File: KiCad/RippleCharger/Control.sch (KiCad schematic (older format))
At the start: 13 parts, among them J3 UART1, J4 UART2, U7 LAUNCHXL-F280049C

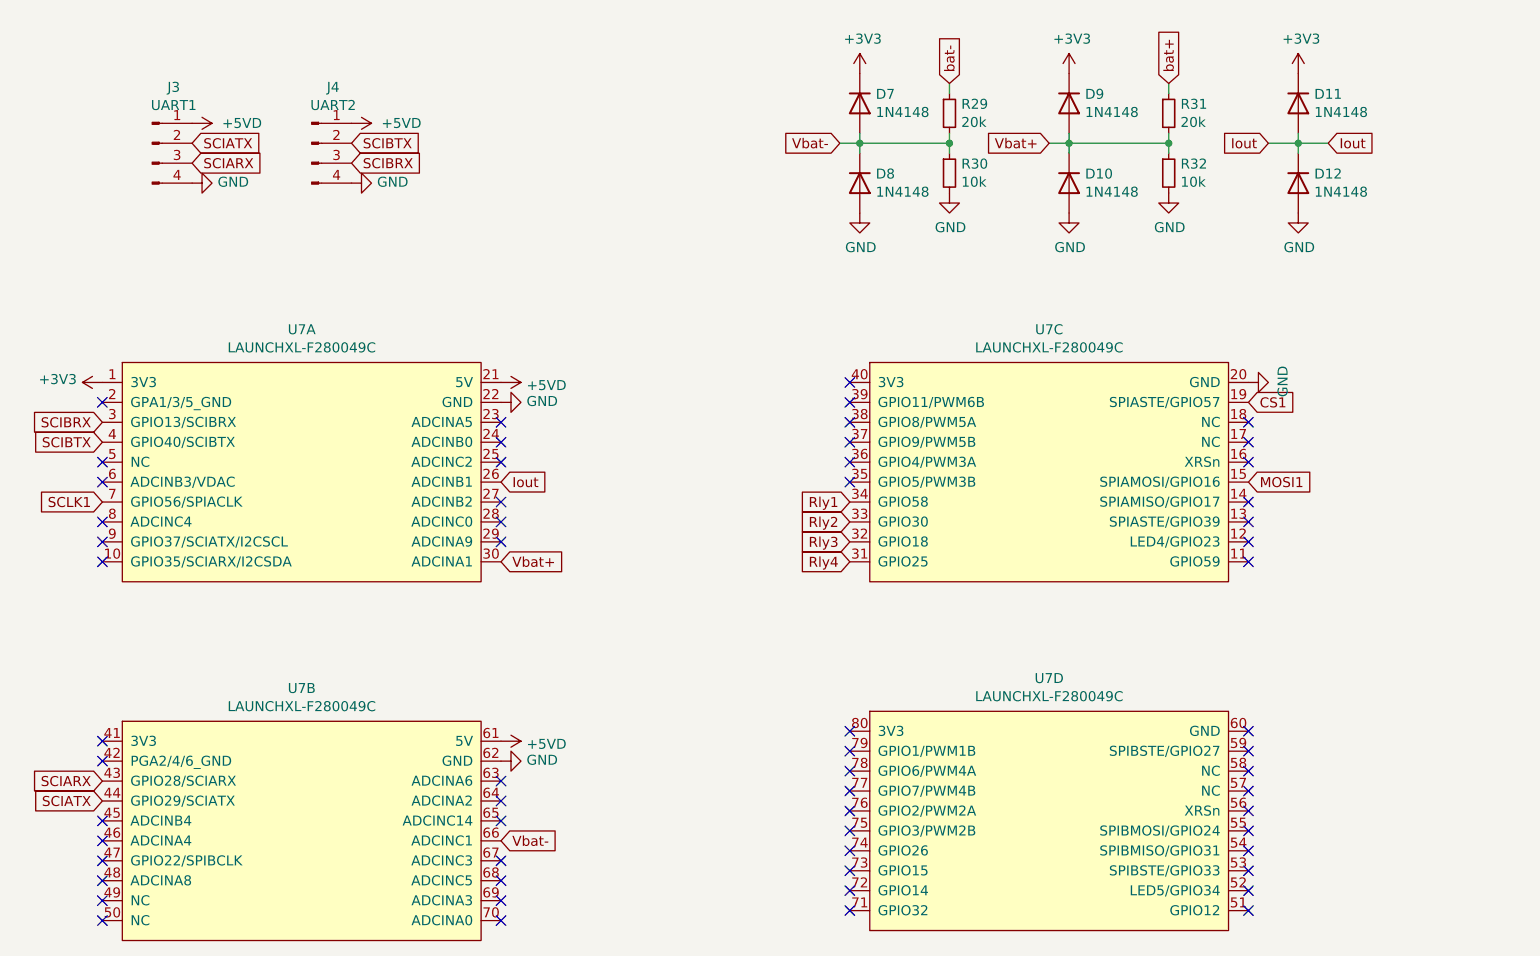
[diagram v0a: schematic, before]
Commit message: Update PCB layout m include relay footprint, board outlook.Modify Main 0049 code and add CV function
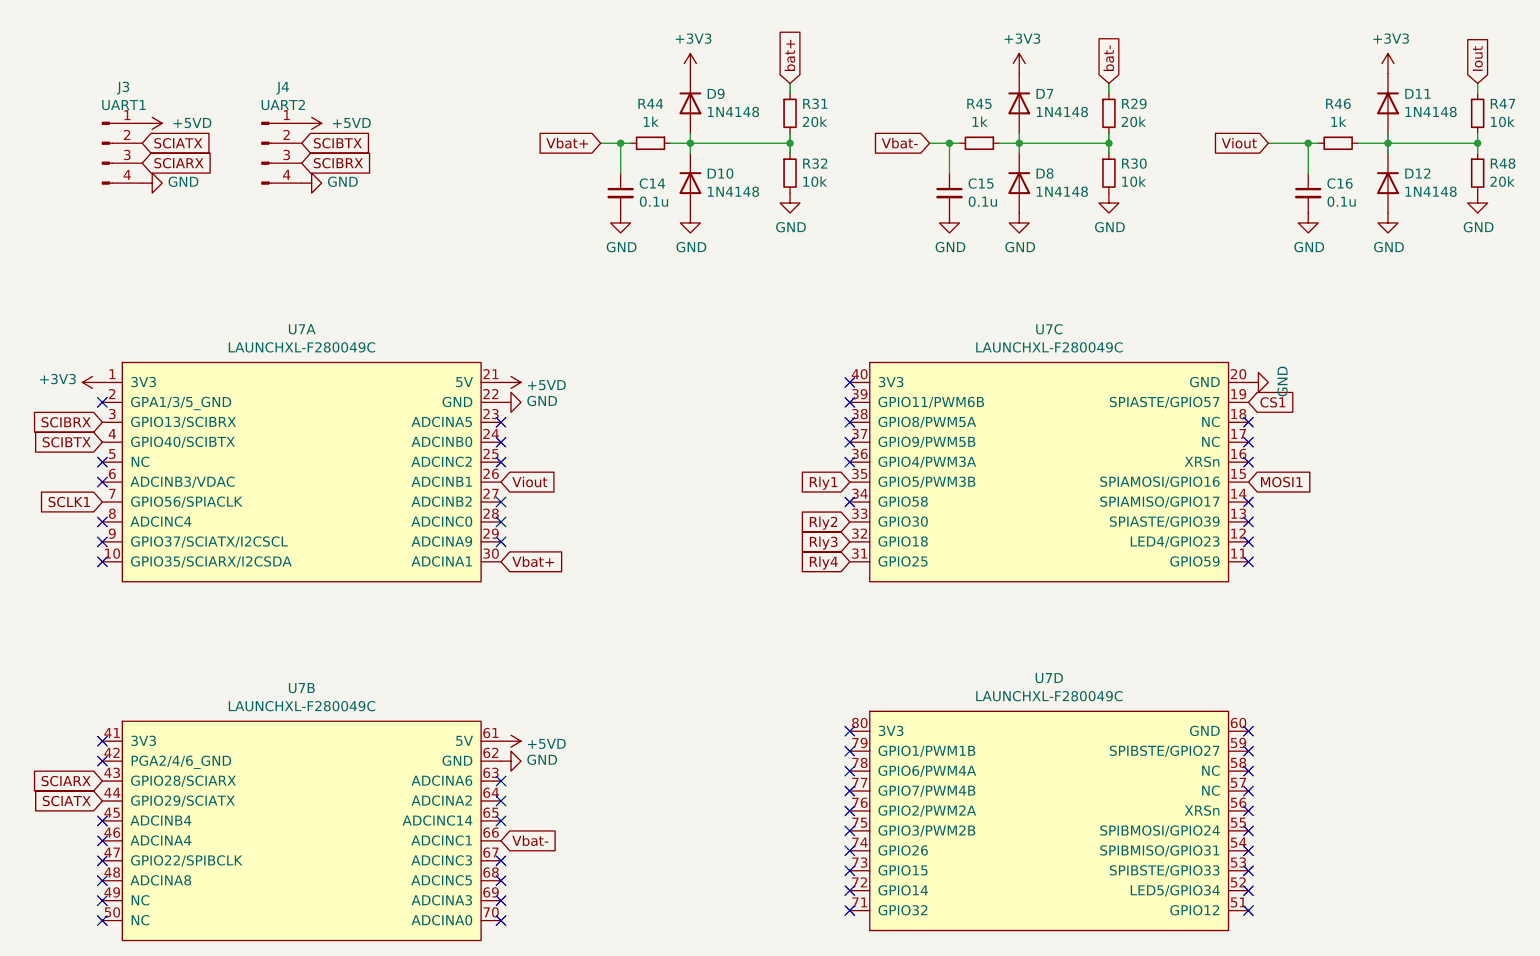
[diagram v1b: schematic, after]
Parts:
- added C14, C15, C16: 0.1u, Capacitor_SMD:C_0805_2012Metric_Pad1.18x1.45mm_HandSolder, symbol Device:C_Small
- added R44, R45, R46: 1k, Resistor_SMD:R_0805_2012Metric_Pad1.20x1.40mm_HandSolder, symbol Device:R_Small
- added R47: 10k, Resistor_SMD:R_0805_2012Metric_Pad1.20x1.40mm_HandSolder, symbol Device:R_Small
- added R48: 20k, Resistor_SMD:R_0805_2012Metric_Pad1.20x1.40mm_HandSolder, symbol Device:R_Small
- D10, D11, D12, D7, D8, D9: footprint Diode_SMD:D_0805_2012Metric_Pad1.15x1.40mm_HandSolder -> Diode_SMD:D_SOD-123
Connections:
- net GND: now also C14.2, C15.2, C16.2, R48.2
- net Iout: now also R47.1; no longer D11.2 (A), D12.1 (K), U7.26 (ADCINB1)
- net Rly1: now also U7.35 (GPIO5/PWM3B); no longer U7.34 (GPIO58)
- net Vbat+: now also C14.1, R44.2; no longer D10.1 (K), D9.2 (A), R31.2, R32.1
- net Vbat-: now also C15.1, R45.2; no longer D7.2 (A), D8.1 (K), R29.2, R30.1
- new net: D7.2 (A), D8.1 (K), R29.2, R30.1, R45.1
- new net: D10.1 (K), D9.2 (A), R31.2, R32.1, R44.1
- new net: D11.2 (A), D12.1 (K), R46.1, R47.2, R48.1
- new net Viout: C16.1, R46.2, U7.26 (ADCINB1)
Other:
- moved on the sheet: D10, D11, D12, D7, D8, D9, J3, J4, R29, R30, R31, R32

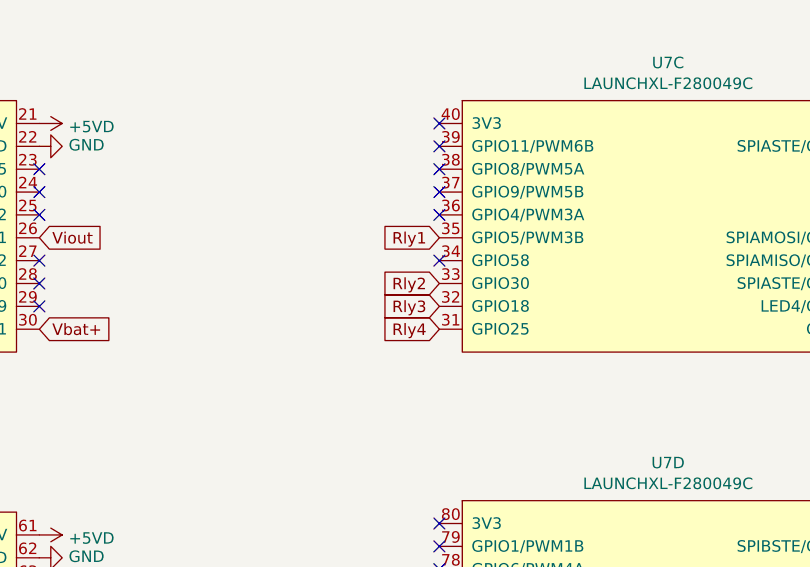
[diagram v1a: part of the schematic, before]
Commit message: Fix CV charging route
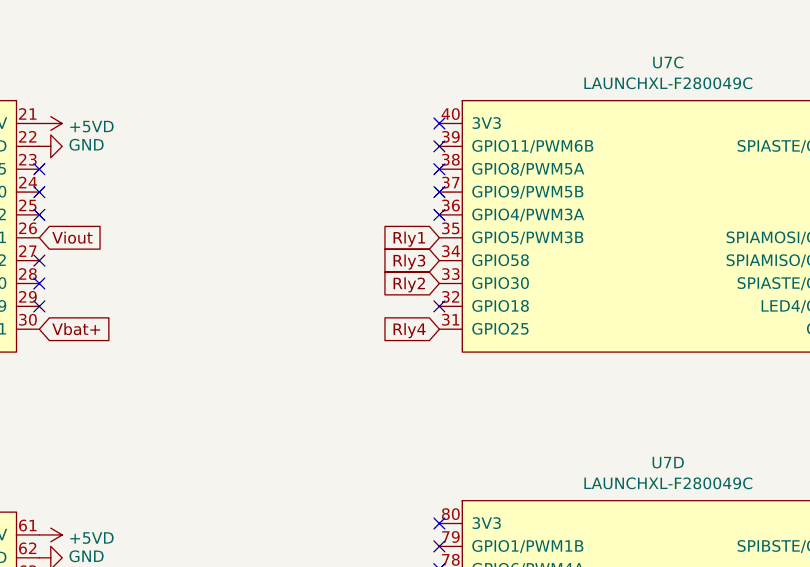
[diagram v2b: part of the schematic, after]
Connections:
- net Rly3: now also U7.34 (GPIO58); no longer U7.32 (GPIO18)
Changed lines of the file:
@@
 Text GLabel 4750 3550 2    50   Input ~ 0
 Viout
-Text GLabel 6500 3850 0    50   Input ~ 0
+Text GLabel 6500 3650 0    50   Input ~ 0
 Rly3
 $Comp
@@
 	1    0    0    -1
 $EndComp
-NoConn ~ 6500 3650
 Wire Wire Line
 	8800 2000 8800 1850
@@
 Wire Wire Line
 	7000 1850 7050 1850
+NoConn ~ 6500 3850
 $EndSCHEMATC
